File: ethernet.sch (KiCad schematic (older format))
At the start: 31 parts, among them U1 DP83848JSQ_NOPB, Y2 ABM8G-25.000MHZ-18-D2Y-T

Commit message: Cleanup around Ethernet schematic
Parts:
- R4, R5, R6, R7, Y2: DNP (none) -> DNP; Populate DNP -> (none)
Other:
- moved on the sheet: C10, R127, R15, R16, R3, R4, R5, R6, R8

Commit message: Add net labels to coupled PCIe lanes
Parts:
- gave numbers to parts that had none: 1
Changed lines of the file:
@@
 	10075 3800 9825 3800
 $Comp
-L artix-dc-scm:RJMG1BD3B8K1ANR J?
+L artix-dc-scm:RJMG1BD3B8K1ANR J1
 U 1 1 5FEA9709
 P 12500 3800
-F 0 "J?" H 13180 3839 50  0000 L CNN
+F 0 "J1" H 13180 3839 50  0000 L CNN
 F 1 "RJMG1BD3B8K1ANR" H 13180 3748 50  0000 L CNN
 F 2 "CONN_RJMG1BD3B8K1ANR" H 12500 4900 50  0001 L BNN

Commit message: Change M.2 description in README
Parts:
- removed J1: RJMG1BD3B8K1ANR, CONN_RJMG1BD3B8K1ANR, symbol artix-dc-scm:RJMG1BD3B8K1ANR
- added J1: WE-RJ45_7499111121A, artix-dc-scm-footprints:7499111121A, symbol artix-dc-scm:WE-RJ45_7499111121A
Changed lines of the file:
@@
-$Comp
-L artix-dc-scm:GND-artix-dc-scm #PWR?
-U 1 1 5FF52D60
-P 12700 4600
-AR Path="/5FE270C1/5FF52D60" Ref="#PWR?"  Part="1"
-AR Path="/60570C04/5FF52D60" Ref="#PWR095"  Part="1"
-F 0 "#PWR095" H 12700 4350 50  0001 C CNN
-F 1 "GND" H 12705 4427 50  0000 C CNN
-F 2 "" H 12700 4600 50  0001 C CNN
-F 3 "" H 12700 4600 50  0001 C CNN
-	1    12700 4600
-	-1   0    0    -1
-$EndComp
 $Comp
 L artix-dc-scm:GND-artix-dc-scm #PWR?
@@
 	10075 3800 9825 3800
 $Comp
-L artix-dc-scm:RJMG1BD3B8K1ANR J1
-U 1 1 5FEA9709
-P 12500 3800
-F 0 "J1" H 13180 3839 50  0000 L CNN
-F 1 "RJMG1BD3B8K1ANR" H 13180 3748 50  0000 L CNN
-F 2 "CONN_RJMG1BD3B8K1ANR" H 12500 4900 50  0001 L BNN
-F 3 "" H 12500 3800 50  0001 L BNN
-F 4 "Amphenol Commercial Products" H 12500 4900 50  0001 L BNN "MANUFACTURER"
-	1    12500 3800
+L artix-dc-scm:WE-RJ45_7499111121A J1
+U 1 1 60294361
+P 13000 5975
+F 0 "J1" H 13100 6840 50  0000 C CNN
+F 1 "WE-RJ45_7499111121A" H 13100 6749 50  0000 C CNN
+F 2 "artix-dc-scm-footprints:7499111121A" H 13000 5975 50  0001 L BNN
+F 3 "" H 13000 5975 50  0001 L BNN
+F 4 "7499111121A" H 13000 5975 50  0001 L BNN "MPN"
+F 5 "WURTH ELEKTRONIK" H 13000 5975 50  0001 C CNN "Manufacturer"
+	1    13000 5975
 	1    0    0    -1
 $EndComp

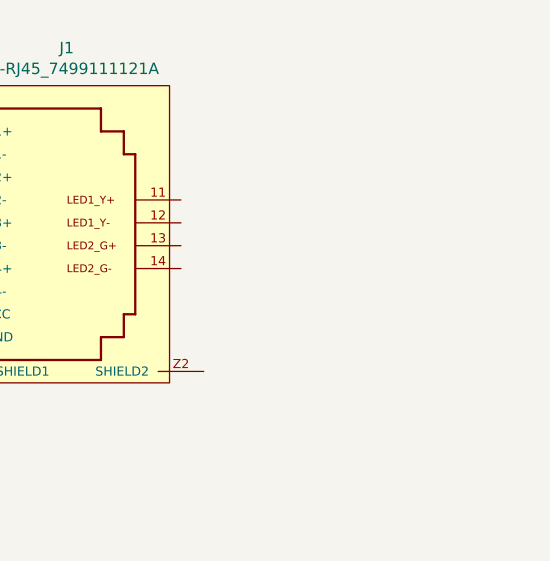
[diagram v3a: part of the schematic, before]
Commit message: Specify eMMC model
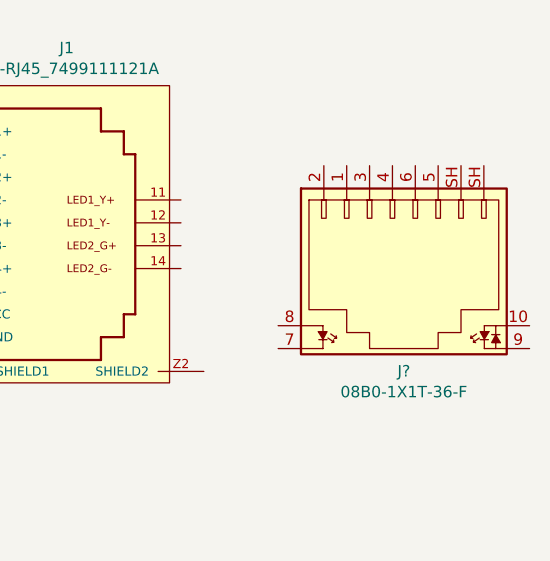
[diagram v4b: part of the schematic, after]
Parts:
- added J?: 08B0-1X1T-36-F, antmicro-footprints:BEL_08B0-1X1T-36-F, symbol antmicroModularConnectorsJacksWithMagnetics:08B0-1X1T-36-F
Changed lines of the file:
@@
+	1    0    0    -1
+$EndComp
+$Comp
+L antmicroModularConnectorsJacksWithMagnetics:08B0-1X1T-36-F J?
+U 1 1 5FEC7CFD
+P 14525 6025
+F 0 "J?" H 14575 5526 50  0000 C CNN
+F 1 "08B0-1X1T-36-F" H 14575 5435 50  0000 C CNN
+F 2 "antmicro-footprints:BEL_08B0-1X1T-36-F" H 14725 6225 50  0001 L CNN
+F 3 "" H 14725 6325 60  0001 L CNN
+F 4 "08B0-1X1T-36-F" H 15075 6475 60  0001 L CNN "MPN"
+F 5 "Abracon LLC" H 14725 7125 60  0001 L CNN "Manufacturer"
+	1    14525 6025
 	1    0    0    -1
 $EndComp

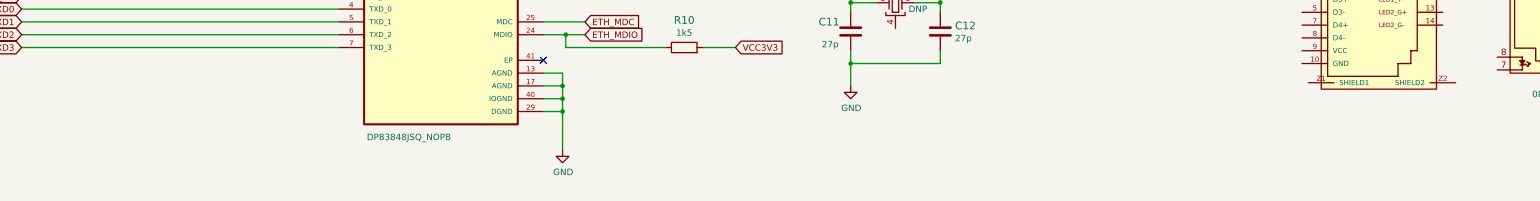
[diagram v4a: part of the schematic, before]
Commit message: Add suggested MPS for ETH PHYs
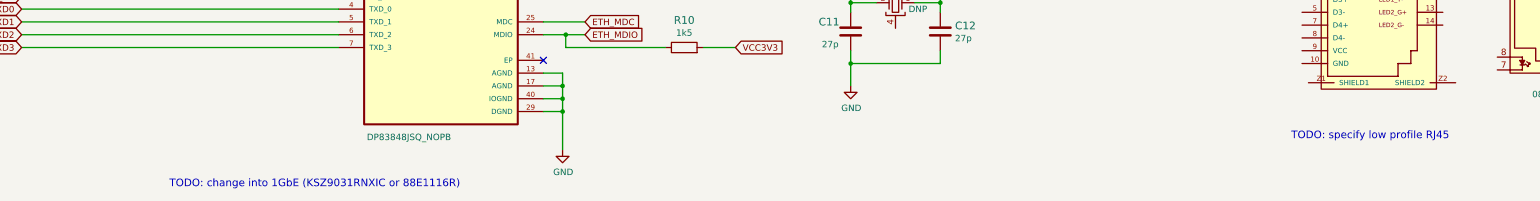
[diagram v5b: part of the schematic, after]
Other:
- note added: "TODO: change into 1GbE (KSZ9031RNXIC or 88E1116R)"
- note added: "TODO: specify low profile RJ45"
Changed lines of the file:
@@
 	1    0    0    -1
 $EndComp
+Text Notes 13650 6975 2    59   ~ 0
+TODO: specify low profile RJ45
+Text Notes 5925 7350 2    59   ~ 0
+TODO: change into 1GbE (KSZ9031RNXIC or 88E1116R)
 $EndSCHEMATC

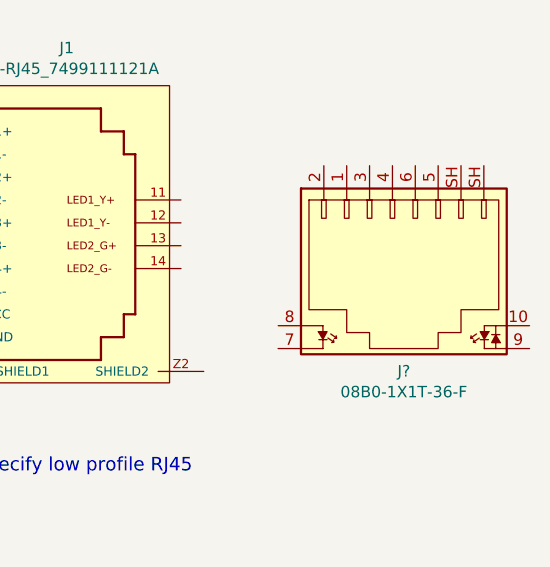
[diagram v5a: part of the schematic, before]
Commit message: Define USB diff lanes
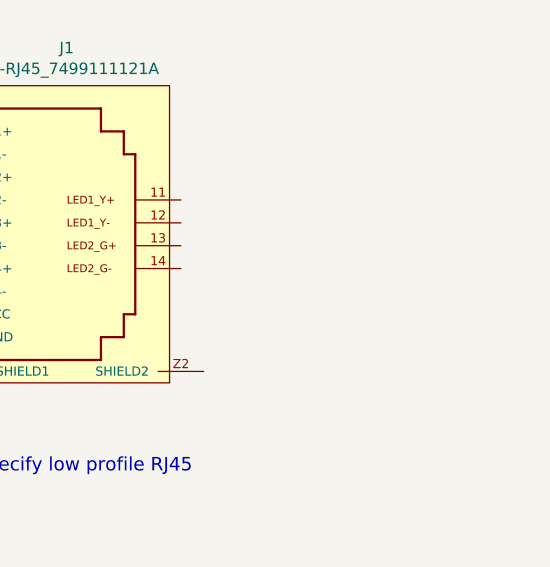
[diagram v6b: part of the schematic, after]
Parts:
- removed J?: 08B0-1X1T-36-F, antmicro-footprints:BEL_08B0-1X1T-36-F, symbol antmicroModularConnectorsJacksWithMagnetics:08B0-1X1T-36-F
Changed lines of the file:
@@
-	1    0    0    -1
-$EndComp
-$Comp
-L antmicroModularConnectorsJacksWithMagnetics:08B0-1X1T-36-F J?
-U 1 1 5FEC7CFD
-P 14525 6025
-F 0 "J?" H 14575 5526 50  0000 C CNN
-F 1 "08B0-1X1T-36-F" H 14575 5435 50  0000 C CNN
-F 2 "antmicro-footprints:BEL_08B0-1X1T-36-F" H 14725 6225 50  0001 L CNN
-F 3 "" H 14725 6325 60  0001 L CNN
-F 4 "08B0-1X1T-36-F" H 15075 6475 60  0001 L CNN "MPN"
-F 5 "Abracon LLC" H 14725 7125 60  0001 L CNN "Manufacturer"
-	1    14525 6025
 	1    0    0    -1
 $EndComp

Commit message: Swapped PHY, P-MOSFETs fix
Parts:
- removed C10, C13, C3, C4, C5, C9: C_100n_0402, artix-dc-scm-footprints:0402-cap, symbol artix-dc-scm:C_100n_0402
- removed C11, C12: C_27p_0402, artix-dc-scm-footprints:0402-cap, symbol artix-dc-scm:C_27p_0402
- removed C2, C6, C7: C_10u_0603, artix-dc-scm-footprints:0603-cap, symbol artix-dc-scm:C_10u_0603
- removed C8: C_1u_0402, artix-dc-scm-footprints:0402-cap, symbol artix-dc-scm:C_1u_0402
- removed FB2: MPZ2012S601AT000, artix-dc-scm-footprints:0805-res, symbol artix-dc-scm:MPZ2012S601AT000
- removed R10: R_1k5_0402, artix-dc-scm-footprints:0402-res, symbol artix-dc-scm:R_1k5_0402
- removed R11: R_0R_0402, artix-dc-scm-footprints:0402-res, symbol artix-dc-scm:R_0R_0402
- removed R3, R4, R5, R6, R7: R_2k2_0402, artix-dc-scm-footprints:0402-res, symbol artix-dc-scm:R_2k2_0402
- removed R8: R_4k87_0402, artix-dc-scm-footprints:0402-res, symbol artix-dc-scm:R_4k87_0402
- removed R9: R_10k_0402, artix-dc-scm-footprints:0402-res, symbol artix-dc-scm:R_10k_0402
- removed U1: DP83848JSQ_NOPB, artix-dc-scm-footprints:DP83848JSQ-NOPB, symbol artix-dc-scm:DP83848JSQ_NOPB
- removed Y2: ABM8G-25.000MHZ-18-D2Y-T, artix-dc-scm-footprints:KX-7, symbol artix-dc-scm:ABM8G-25.000MHZ-18-D2Y-T
- added C196, C198, C199, C200, C206: C_4u7_0402, antmicro-footprints:0402-cap, symbol antmicroCapacitors0402:C_4u7_0402
- added C197, C201, C202, C204, C205: C_470n_0402, antmicro-footprints:0402-cap, symbol antmicroCapacitors0402:C_470n_0402
- added C2, C3: C_1u_0402, antmicro-footprints:0402-cap, symbol antmicroCapacitors0402:C_1u_0402
- added C203: C_100n_0402, antmicro-footprints:0402-cap, symbol antmicroCapacitors0402:C_100n_0402
- added C207, C208, C209, C210, C211, C212, C213, C214, C215, C216, C217, C218, C219: C_10n_0402, antmicro-footprints:0402-cap, symbol antmicroCapacitors0402:C_10n_0402
- added C220, C221: C_22p_0402, antmicro-footprints:0402-cap, symbol antmicroCapacitors0402:C_22p_0402
- added FB4, FB5, FB6: BLM18PG121SN1D, antmicro-footprints:0603-res, symbol antmicroFerriteBeadsandChips:BLM18PG121SN1D
- added IC2: TLV73312PDBVT, antmicro-footprints:SOT-23-5, symbol antmicroPMICVoltageRegulatorsLinear:TLV73312PDBVT
- added R127, R148, R149, R150, R151, R152, R153, R154, R155, R156, R157, R158: R_10k2_0402, antmicro-footprints:0402-res, symbol antmicroResistors0402:R_10k2_0402
- added R159: R_12k1_0402, antmicro-footprints:0402-res, symbol antmicroResistors0402:R_12k1_0402
- added R160: R_1M8_0402, antmicro-footprints:0402-res, symbol antmicroResistors0402:R_1M8_0402
- added U20: KSZ9031RNXCA, antmicro-footprints:QFN-48-Microchip-QFN77-48LD-PL-2, symbol antmicroInterfaceControllers:KSZ9031RNXCA
- added Y2: ABM8G-25.000MHZ-18-D2Y-T, antmicro-footprints:KX-7, symbol antmicroCrystals:ABM8G-25.000MHZ-18-D2Y-T
- renumbered J1 to J8, R127 to R161, R16 to R162, R15 to R163, R14 to R164, R12 to R165, R13 to R166
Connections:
- net labels added: AVDDH, AVDDL, AVDDL_PLL, DVDDH, DVDDL, ETH1_N, ETH1_P, ETH2_N, ETH2_P, ETH3_N, ETH3_P, ETH4_N, ETH4_P, ETH_INT_N, ETH_LED1, ETH_LED2, ETH_~RESET, RGMII_REF_CLK, RGMII_RXD0, RGMII_RXD1, RGMII_RXD2, RGMII_RXD3, RGMII_RX_CLK, RGMII_RX_DV, RGMII_TXD0, RGMII_TXD1, RGMII_TXD2, RGMII_TXD3, RGMII_TX_CLK, RGMII_TX_DV, VCC1V2
- net labels removed: ETH_COL, ETH_CRS, ETH_REF_CLK, ETH_RSTN, ETH_RXD0, ETH_RXD1, ETH_RXD2, ETH_RXD3, ETH_RXERR, ETH_RX_CLK, ETH_RX_DV, ETH_TXD0, ETH_TXD1, ETH_TXD2, ETH_TXD3, ETH_TX_CLK, ETH_TX_EN, PFBOUT, RXN, RXP, TXN, TXP
- wire segments 160 -> 258
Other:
- note added: "1V2 LDO"
- note added: "AVDDH decoupling"
- note added: "AVDDL decoupling"
- note added: "AVDDL_PLL decoupling"
- note added: "DVDDH decoupling"
- note added: "DVDDL decoupling"
- note added: "PHY"
- note added: "Pull up resistors"
- note removed: "Ethernet transceiver"
- note removed: "TODO: change into 1GbE (KSZ9031RNXIC or 88E1116R)"
- moved on the sheet: J8, R161, R162, R163, R164, R165, R166

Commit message: Replaced and connected eMMC, replaced RJ45
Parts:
- removed J8: WE-RJ45_7499111121A, artix-dc-scm-footprints:7499111121A, symbol artix-dc-scm:WE-RJ45_7499111121A
- removed R161, R162, R163, R164: R_49R9_0402, artix-dc-scm-footprints:0402-res, symbol artix-dc-scm:R_49R9_0402
- added C225, C226, C227, C228: C_100n_0402, antmicro-footprints:0402-cap, symbol antmicroCapacitors0402:C_100n_0402
- added J1: L834-1G1T-S7, antmicro-footprints:BEL_L834-1G1T-S7, symbol antmicroModularConnectorsJacksWithMagnetics:L834-1G1T-S7
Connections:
- net labels removed: ETH3V3
- wire segments 258 -> 254
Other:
- note removed: "TODO: specify low profile RJ45"
- moved on the sheet: R165, R166
